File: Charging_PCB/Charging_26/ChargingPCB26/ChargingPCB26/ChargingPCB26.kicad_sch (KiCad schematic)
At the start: 58 parts, among them J1 Molex6pin, J2 Molex6pin, K101 Relay_SPDT_Omron_G2RL-1, K102 Relay_SPDT_Omron_G2RL-1, Q1 NMOS, Q103 Q_NPN_BEC, Q104 Q_NPN_BEC, Q105 Q_NPN_BEC, Q106 Q_NPN_BEC, Q2 NMOS, Q3 NMOS, Q4 NMOS, SW101 SW_Omron_B3FS, SW102 SW_Omron_B3FS, U1 SFH617A-1, U107 LM7805_TO220, U2 SFH617A-1, U5 74LS279, U6 74HC00

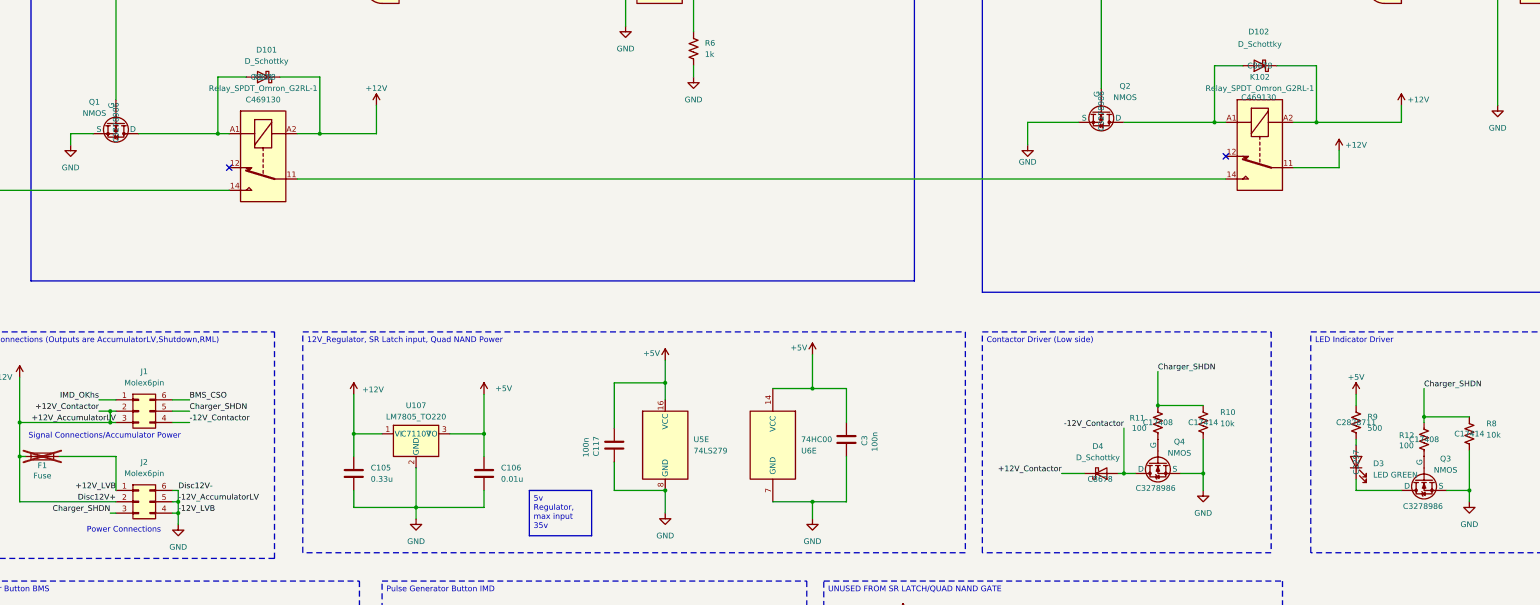
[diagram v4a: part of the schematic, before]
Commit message: Charging FIxes
NMOS's Q1-4 had the wrong symbol as DGS, updated symbol and board with NMOS's Q1-4 to now have the correct symbol of GDS, to match the datasheet.
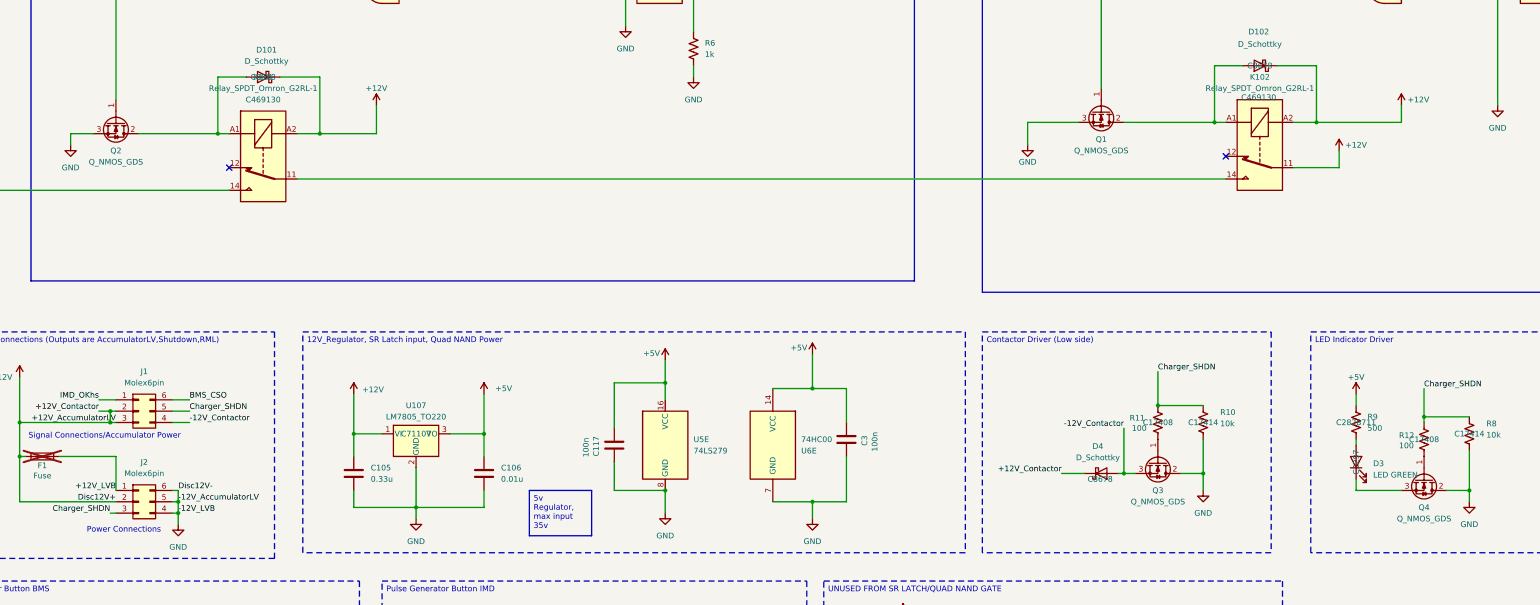
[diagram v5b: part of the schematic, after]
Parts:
- removed Q1, Q2, Q3, Q4: NMOS, Package_TO_SOT_THT:TO-251-3_Vertical, symbol Simulation_SPICE:NMOS
- added Q1, Q2, Q3, Q4: Q_NMOS_GDS, Package_TO_SOT_THT:TO-251-3_Vertical, symbol Transistor_FET:Q_NMOS_GDS
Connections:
- net -12V_Contactor: now also Q3.3 (S)
- net GND: now also Q1.3 (S), Q2.3 (S), Q3.2 (D), Q4.2 (D)
- net at D1.1 (K), U5.4 (Q): now also Q2.1 (G)
- net at D101.2 (A), K101.A1: now also Q2.2 (D)
- net at D102.2 (A), K102.A1: now also Q1.2 (D)
- net at D2.1 (K), U5.9 (Q): now also Q1.1 (G)
- net at D3.1 (K): now also Q4.3 (S)
- net at R12.2: now also Q4.1 (G)
- net at R11.2: now also Q3.1 (G)

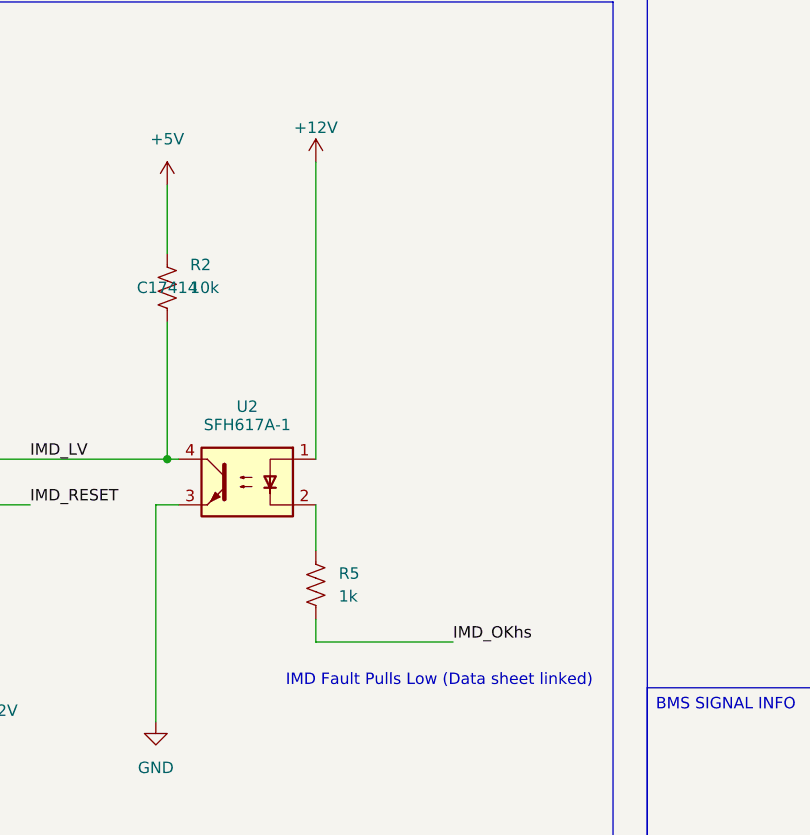
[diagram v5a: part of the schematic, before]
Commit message: Charging fixes
added pull down resistor to imd signal so it faults when unconnected
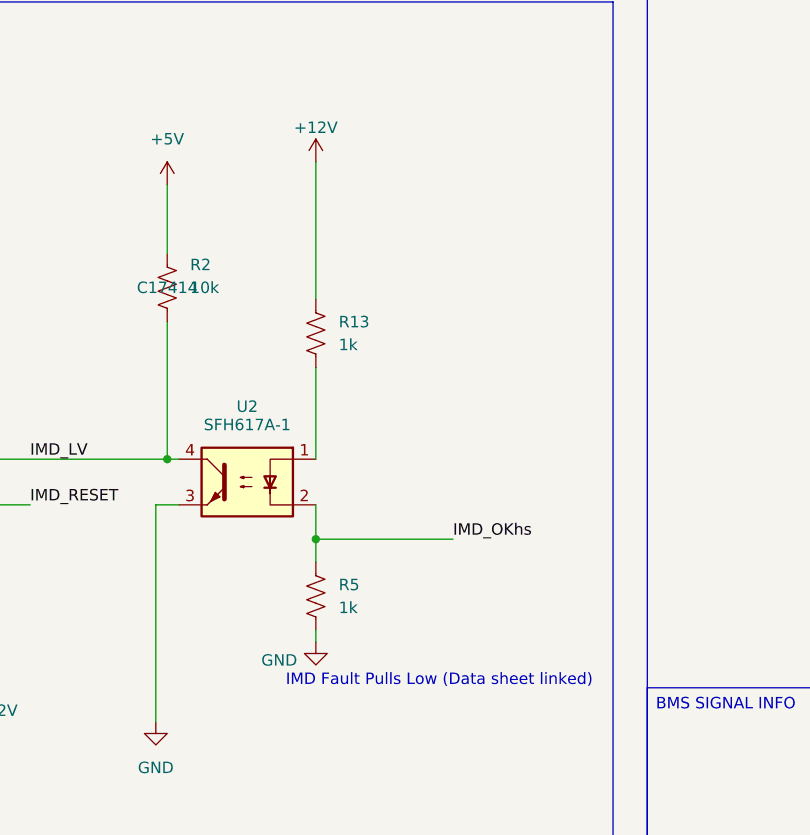
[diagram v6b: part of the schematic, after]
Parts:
- added R13: 1k, Resistor_SMD:R_0805_2012Metric_Pad1.20x1.40mm_HandSolder, symbol Device:R_US
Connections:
- net +12V: now also R13.1; no longer U2.1
- net GND: now also R5.2
- net IMD_OKhs: now also R5.1, U2.2; no longer R5.2
- new net: R13.2, U2.1
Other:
- moved on the sheet: R5
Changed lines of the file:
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@@
 	)
 	(junction
+		(at 398.78 106.68)
+		(diameter 0)
+		(color 0 0 0 0)
+	)
+	(junction
 		(at 328.93 100.33)
 		(diameter 0)
@@
 	(wire
 		(pts
+			(xy 398.78 106.68) (xy 398.78 109.22)
+		)
+		(stroke
+			(width 0)
+			(type default)
+		)
+	)
+	(wire
+		(pts
 			(xy 307.34 262.89) (xy 298.45 262.89)
 		)
@@
 	(wire
 		(pts
-			(xy 398.78 102.87) (xy 398.78 107.95)
-		)
-		(stroke
-			(width 0)
-			(type default)
-		)
-	)
-	(wire
-		(pts
 			(xy 71.12 198.12) (xy 69.85 198.12)
 		)
@@
 	(wire
 		(pts
-			(xy 398.78 97.79) (xy 398.78 64.77)
-		)
-		(stroke
-			(width 0)
-			(type default)
-		)
-	)
-	(wire
-		(pts
 			(xy 129.54 133.35) (xy 116.84 133.35)
 		)
@@
 	(wire
 		(pts
+			(xy 398.78 102.87) (xy 398.78 106.68)
+		)
+		(stroke
+			(width 0)
+			(type default)
+		)
+	)
+	(wire
+		(pts
 			(xy 292.1 97.79) (xy 292.1 93.98)
 		)
@@
 	(wire
 		(pts
+			(xy 398.78 116.84) (xy 398.78 118.11)
+		)
+		(stroke
+			(width 0)
+			(type default)
+		)
+	)
+	(wire
+		(pts
 			(xy 364.49 196.85) (xy 364.49 198.12)
 		)
@@
 	(wire
 		(pts
-			(xy 398.78 118.11) (xy 414.02 118.11)
+			(xy 398.78 87.63) (xy 398.78 97.79)
 		)
 		(stroke
@@
 	(wire
 		(pts
-			(xy 398.78 115.57) (xy 398.78 118.11)
+			(xy 398.78 106.68) (xy 414.02 106.68)
 		)
 		(stroke
@@
 	(wire
 		(pts
+			(xy 398.78 64.77) (xy 398.78 80.01)
+		)
+		(stroke
+			(width 0)
+			(type default)
+		)
+	)
+	(wire
+		(pts
 			(xy 189.23 262.89) (xy 189.23 265.43)
 		)
@@
 	)
 	(label "IMD_OKhs"
-		(at 414.02 118.11 0)
+		(at 414.02 106.68 0)
 		(effects
 			(font
@@
 	(symbol
 		(lib_id "Device:R_US")
-		(at 398.78 111.76 0)
+		(at 398.78 113.03 0)
 		(unit 1)
 		(exclude_from_sim no)
@@
 		(fields_autoplaced yes)
 		(property "Reference" "R5"
-			(at 401.32 110.4899 0)
+			(at 401.32 111.7599 0)
 			(effects
 				(font
@@
 		)
 		(property "Value" "1k"
-			(at 401.32 113.0299 0)
+			(at 401.32 114.2999 0)
 			(effects
 				(font
@@
 		)
 		(property "Footprint" "Resistor_SMD:R_0805_2012Metric_Pad1.20x1.40mm_HandSolder"
-			(at 399.796 112.014 90)
+			(at 399.796 113.284 90)
 			(effects
 				(font
@@
 		)
 		(property "Datasheet" "https://jlcpcb.com/api/file/downloadByFileSystemAccessId/8579706499683172352"
-			(at 398.78 111.76 0)
+			(at 398.78 113.03 0)
 			(effects
 				(font
@@
 		)
 		(property "Description" "Resistor, US symbol"
-			(at 398.78 111.76 0)
+			(at 398.78 113.03 0)
 			(effects
 				(font
@@
 		)
 		(property "MPN" "0805W8F1001T5E"
-			(at 398.78 111.76 0)
+			(at 398.78 113.03 0)
 			(effects
 				(font
@@
 		)
 		(property "Digikey" "1.00KXBK-ND"
-			(at 398.78 111.76 0)
+			(at 398.78 113.03 0)
 			(effects
 				(font
@@
 		)
 		(property "JLC#" " C17513"
-			(at 398.78 111.76 0)
+			(at 398.78 113.03 0)
 			(effects
 				(font
@@
 	(symbol
 		(lib_id "power:GND")
+		(at 398.78 118.11 0)
+		(unit 1)
+		(exclude_from_sim no)
+		(in_bom yes)
+		(on_board yes)
+		(dnp no)
+		(property "Reference" "#PWR019"
+			(at 398.78 124.46 0)
+			(effects
+				(font
+					(size 1.27 1.27)
+				)
+				(hide yes)
+			)
+		)
+		(property "Value" "GND"
+			(at 394.716 120.142 0)
+			(effects
+				(font
+					(size 1.27 1.27)
+				)
+			)
+		)
+		(property "Footprint" ""
+			(at 398.78 118.11 0)
+			(effects
+				(font
+					(size 1.27 1.27)
+				)
+				(hide yes)
+			)
+		)
+		(property "Datasheet" ""
+			(at 398.78 118.11 0)
+			(effects
+				(font
+					(size 1.27 1.27)
+				)
+				(hide yes)
+			)
+		)
+		(property "Description" "Power symbol creates a global label with name \"GND\" , ground"
+			(at 398.78 118.11 0)
+			(effects
+				(font
+					(size 1.27 1.27)
+				)
+				(hide yes)
+			)
+		)
+		(pin "1"
+		)
+		(instances
+			(project ""
+				(path "/88650a2b-6e67-4b1c-a95e-ec9c4f40b38b"
+					(reference "#PWR019")
+					(unit 1)
+				)
+			)
+		)
+	)
+	(symbol
+		(lib_id "power:GND")
 		(at 381 127 0)
 		(unit 1)
@@
 					(unit 1)
 				)
+			)
+		)
+	)
+	(symbol
+		(lib_id "Device:R_US")
+		(at 398.78 83.82 0)
+		(unit 1)
+		(exclude_from_sim no)
+		(in_bom yes)
+		(on_board yes)
+		(dnp no)
+		(fields_autoplaced yes)
+		(property "Reference" "R13"
+			(at 401.32 82.5499 0)
+			(effects
+				(font
+					(size 1.27 1.27)
+				)
+				(justify left)
+			)
+		)
+		(property "Value" "1k"
+			(at 401.32 85.0899 0)
+			(effects
+				(font
+					(size 1.27 1.27)
+				)
+				(justify left)
+			)
+		)
+		(property "Footprint" "Resistor_SMD:R_0805_2012Metric_Pad1.20x1.40mm_HandSolder"
+			(at 399.796 84.074 90)
+			(effects
+				(font
+					(size 1.27 1.27)
+				)
+				(hide yes)
+			)
+		)
+		(property "Datasheet" "https://jlcpcb.com/api/file/downloadByFileSystemAccessId/8579706499683172352"
+			(at 398.78 83.82 0)
+			(effects
+				(font
+					(size 1.27 1.27)
+				)
+				(hide yes)
+			)
+		)
+		(property "Description" "Resistor, US symbol"
+			(at 398.78 83.82 0)
+			(effects
+				(font
+					(size 1.27 1.27)
+				)
+				(hide yes)
+			)
+		)
+		(property "MPN" "0805W8F1001T5E"
+			(at 398.78 83.82 0)
+			(effects
+				(font
+					(size 1.27 1.27)
+				)
+				(hide yes)
+			)
+		)
+		(property "Digikey" "1.00KXBK-ND"
+			(at 398.78 83.82 0)
+			(effects
+				(font
+					(size 1.27 1.27)
+				)
+				(hide yes)
+			)
+		)
+		(property "JLC#" " C17513"
+			(at 398.78 83.82 0)
+			(effects
+				(font
+					(size 1.27 1.27)
+				)
+				(hide yes)
+			)
+		)
+		(pin "2"
+		)
+		(pin "1"
+		)
+		(instances
+			(project "ChargingPCB26"
+				(path "/88650a2b-6e67-4b1c-a95e-ec9c4f40b38b"
+					(reference "R13")
+					(unit 1)
+				)

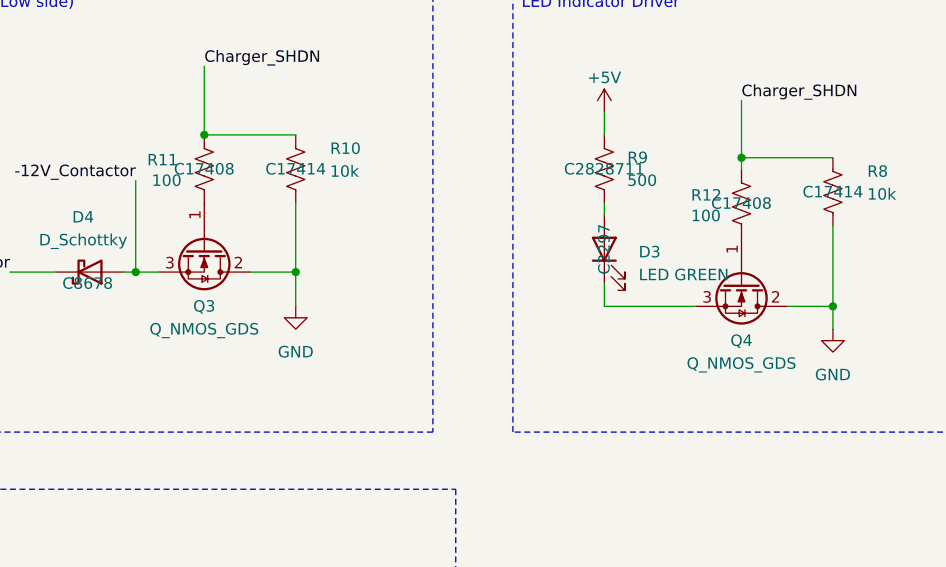
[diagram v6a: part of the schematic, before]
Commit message: charging
fixed issue where Q3 and Q4 mosfets had source and drain swapped
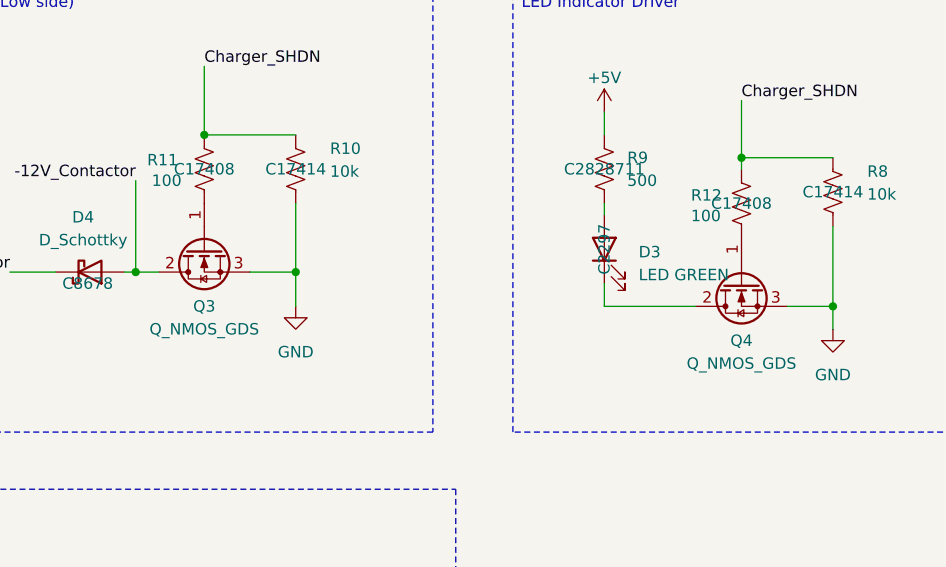
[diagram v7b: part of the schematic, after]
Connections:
- net -12V_Contactor: now also Q3.2 (D); no longer Q3.3 (S)
- net GND: now also Q3.3 (S), Q4.3 (S); no longer Q3.2 (D), Q4.2 (D)
- net at D3.1 (K): now also Q4.2 (D); no longer Q4.3 (S)
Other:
- moved on the sheet: Q3, Q4
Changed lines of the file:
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@@
 	(symbol
 		(lib_id "Transistor_FET:Q_NMOS_GDS")
-		(at 364.49 210.82 270)
+		(at 364.49 210.82 90)
+		(mirror x)
 		(unit 1)
 		(exclude_from_sim no)
@@
 		(on_board yes)
 		(dnp no)
-		(fields_autoplaced yes)
 		(property "Reference" "Q4"
 			(at 364.49 217.17 90)
@@
 		)
 		(property "Footprint" "Package_TO_SOT_THT:TO-251-3_Vertical"
-			(at 367.03 215.9 0)
+			(at 361.95 215.9 0)
 			(effects
 				(font
@@
 	(symbol
 		(lib_id "Transistor_FET:Q_NMOS_GDS")
-		(at 304.8 207.01 270)
+		(at 304.8 207.01 90)
+		(mirror x)
 		(unit 1)
 		(exclude_from_sim no)
@@
 		(on_board yes)
 		(dnp no)
-		(fields_autoplaced yes)
 		(property "Reference" "Q3"
 			(at 304.8 213.36 90)
@@
 		)
 		(property "Footprint" "Package_TO_SOT_THT:TO-251-3_Vertical"
-			(at 307.34 212.09 0)
+			(at 302.26 212.09 0)
 			(effects
 				(font
